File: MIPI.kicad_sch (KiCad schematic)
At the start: 14 parts, among them J14 AFC11-S30ICC-00, J15 AFC11-S30ICC-00

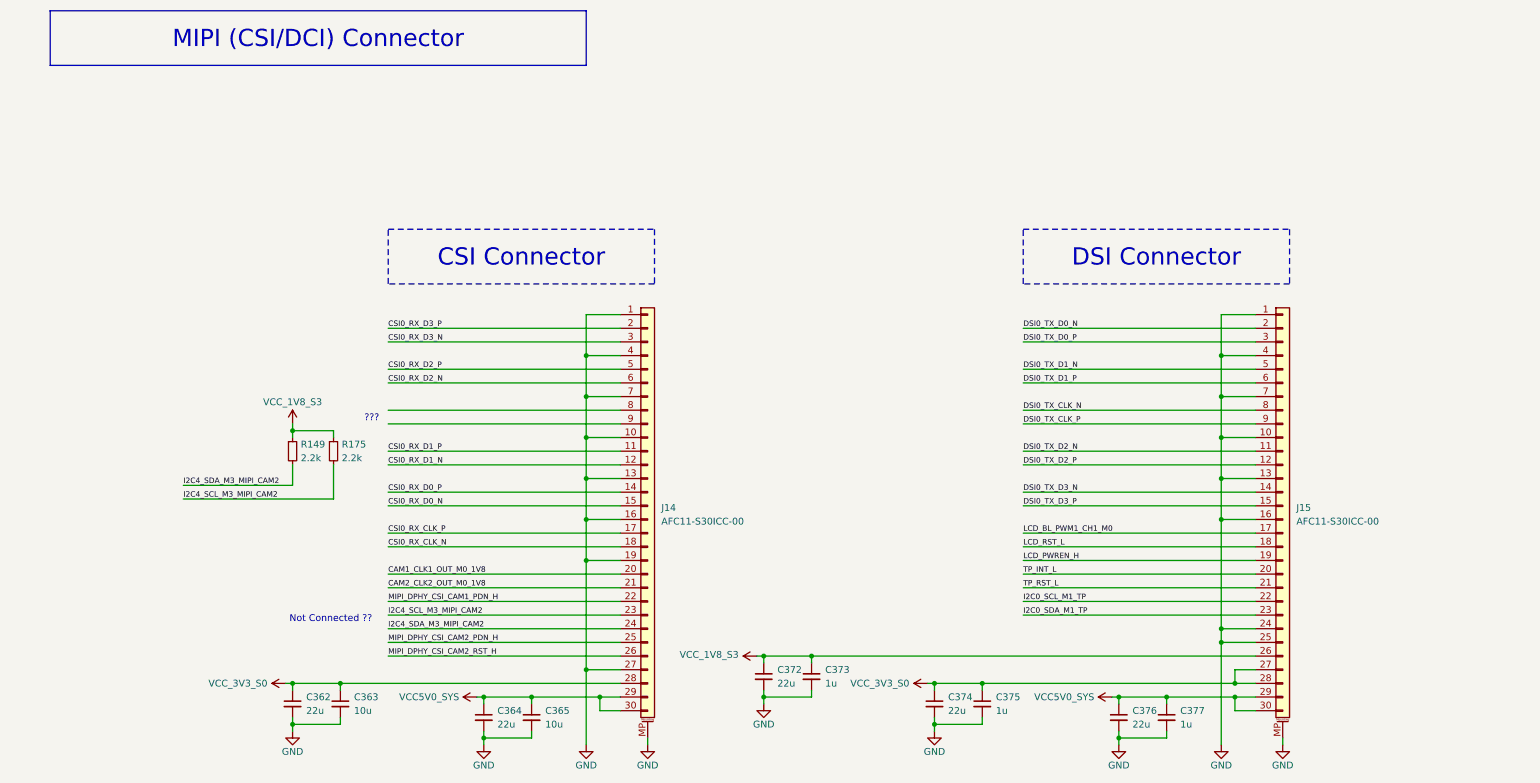
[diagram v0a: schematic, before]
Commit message: Replace v2 with updated RK3576_SBCv2 (Copy) Oct 2
- Update 18 sheets to Oct 2 15:37 local versions
- Keep cleaned layout: exclude .history/, Resources/, *.bak, *.lck,
  project.kicad_dru, .hs_rules.json, lowercase dup placeholders
  (fixtures/power), empty orphans (digital, mechanical, output,
  USBC_MCU, eMMC_UFS)
- Preserve LICENSE, README.md, .gitignore
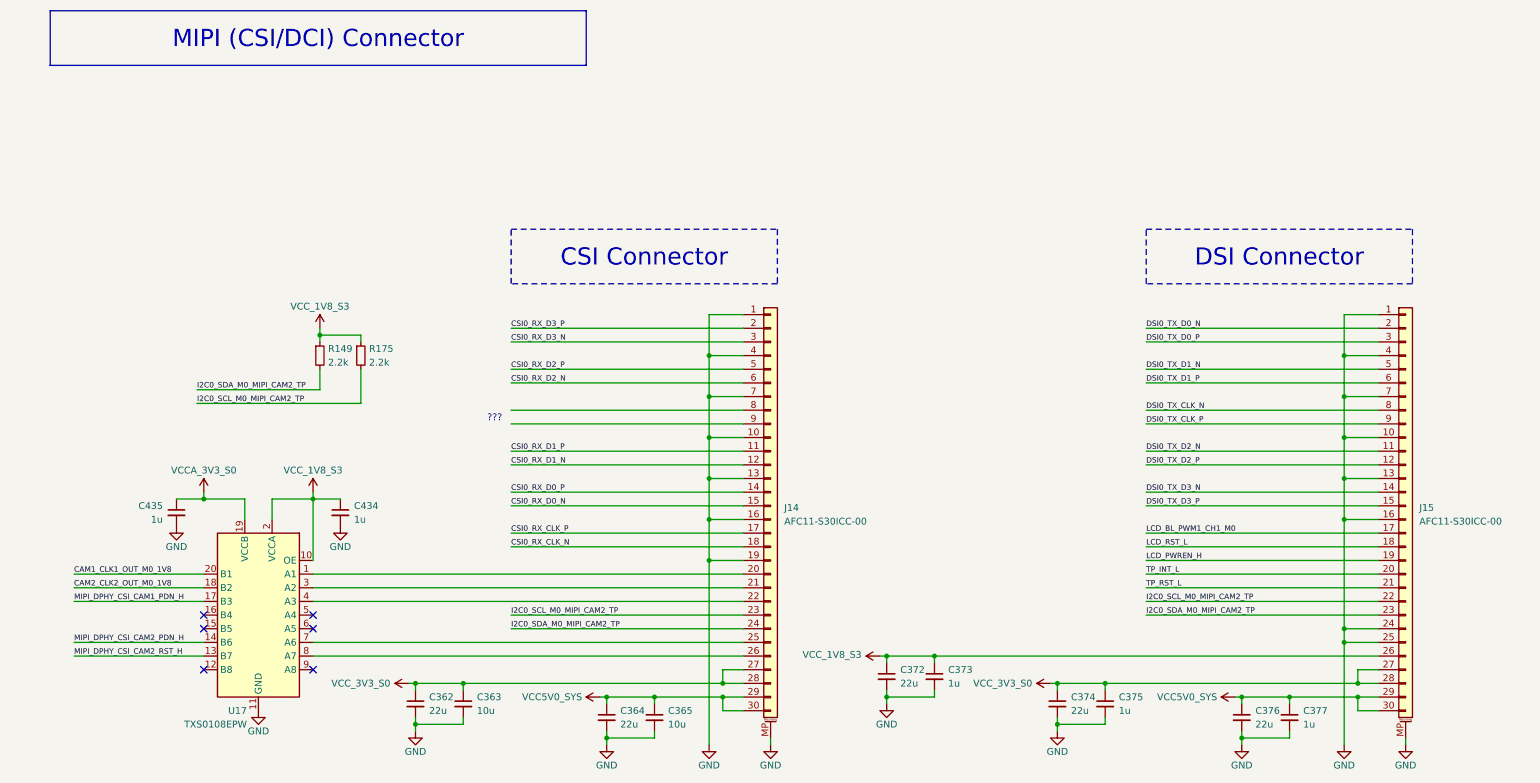
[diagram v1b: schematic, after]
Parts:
- added C434, C435: 1u, Capacitor_SMD:C_0201_0603Metric_Pad0.64x0.40mm_HandSolder, symbol New_Library_0:C_Small_edited
- added U17: TXS0108EPW, Datasheet_Footprints:TXS0108ERGYR_VQFN-20-EP_C90706, symbol Logic_LevelTranslator:TXS0108EPW
- C363, C365: footprint Capacitor_SMD:C_0201_0603Metric_Pad0.64x0.40mm_HandSolder -> Capacitor_SMD:C_0603_1608Metric; LCSC Part C5209398 -> C19702; Mouser Part CL03A105KP3NSNC -> 187-CL10A106KP8NNNC
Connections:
- net I2C4_SCL_M3_MIPI_CAM2 is gone; now on net I2C0_SCL_M0_MIPI_CAM2_TP: J14.23 (Pin_23), R175.2
- net I2C4_SDA_M3_MIPI_CAM2 is gone; now on net I2C0_SDA_M0_MIPI_CAM2_TP: J14.24 (Pin_24), R149.2
- net CAM1_CLK1_OUT_M0_1V8: now also U17.20 (B1); no longer J14.20 (Pin_20)
- net CAM2_CLK2_OUT_M0_1V8: now also U17.18 (B2); no longer J14.21 (Pin_21)
- net GND: now also C434.2, C435.2, U17.11 (GND); no longer J14.27 (Pin_27)
- net MIPI_DPHY_CSI_CAM1_PDN_H: now also U17.17 (B3); no longer J14.22 (Pin_22)
- net MIPI_DPHY_CSI_CAM2_PDN_H: now also U17.14 (B6); no longer J14.25 (Pin_25)
- net MIPI_DPHY_CSI_CAM2_RST_H: now also U17.13 (B7); no longer J14.26 (Pin_26)
- net VCC_1V8_S3: now also C434.1, U17.10 (OE), U17.2 (VCCA)
- net VCC_3V3_S0: now also J14.27 (Pin_27)
- net I2C0_SCL_M1_TP renamed I2C0_SCL_M0_MIPI_CAM2_TP
- net I2C0_SDA_M1_TP renamed I2C0_SDA_M0_MIPI_CAM2_TP
- new net: J14.20 (Pin_20), U17.1 (A1)
- new net: J14.21 (Pin_21), U17.3 (A2)
- new net: J14.22 (Pin_22), U17.4 (A3)
- new net: J14.25 (Pin_25), U17.7 (A6)
- new net: J14.26 (Pin_26), U17.8 (A7)
- new net VCCA_3V3_S0: C435.1, U17.19 (VCCB)
- no-connect marks 0 -> 6
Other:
- note removed: "Not Connected ??"
- moved on the sheet: C362, C363, C364, C365, C372, C373, C374, C375, C376, C377, J14, J15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

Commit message: Relink hierarchical root: 18 sheets into RK3576 SBCv2 top level
Root was empty (no sheet boxes); all subsheets orphaned.
Rebuilt A1 top level linking RK3576, LPDDR5, Power, Ethernet,
HDMI, MIPI, PCIe, USB-A/C, Wireless, RTC, uSD, GPIO, OLED,
RP2350A, Connectors, Fixtures, DC_Power. block_diagrame kept
docs-only (unlinked, avoids double-instantiation). Lowercase
stub duplicates excluded. ERC: 1388 -> 770 violations.
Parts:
- removed J14, J15: AFC11-S30ICC-00, easyeda2kicad:FPC-SMD_30P-L20.5-W2.0-P0.50, symbol Connector_Generic_MountingPin:Conn_01x30_MountingPin
- removed U17: TXS0108EPW, Datasheet_Footprints:TXS0108ERGYR_VQFN-20-EP_C90706, symbol Logic_LevelTranslator:TXS0108EPW
- added J16, J17: AFC11-S30ICC-00, easyeda2kicad:FPC-SMD_30P-L20.5-W2.0-P0.50, symbol Connector_Generic_MountingPin:Conn_01x30_MountingPin
- added U41: TXS0108EPW, Datasheet_Footprints:TXS0108ERGYR_VQFN-20-EP_C90706, symbol Logic_LevelTranslator:TXS0108EPW
- renumbered C435 to C252, C434 to C253, C362 to C254, C363 to C255, C364 to C256, C365 to C257, C372 to C258, C373 to C259, C374 to C260, C375 to C261, C376 to C262, C377 to C263, R149 to R185, R175 to R186
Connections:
- net CAM1_CLK1_OUT_M0_1V8: now also U41.20 (B1)
- net CAM2_CLK2_OUT_M0_1V8: now also U41.18 (B2)
- net CSI0_RX_CLK_N: now also J16.18 (Pin_18)
- net CSI0_RX_CLK_P: now also J16.17 (Pin_17)
- net CSI0_RX_D0_N: now also J16.15 (Pin_15)
- net CSI0_RX_D0_P: now also J16.14 (Pin_14)
- net CSI0_RX_D1_N: now also J16.12 (Pin_12)
- net CSI0_RX_D1_P: now also J16.11 (Pin_11)
- net CSI0_RX_D2_N: now also J16.6 (Pin_6)
- net CSI0_RX_D2_P: now also J16.5 (Pin_5)
- net CSI0_RX_D3_N: now also J16.3 (Pin_3)
- net CSI0_RX_D3_P: now also J16.2 (Pin_2)
- net DSI0_TX_CLK_N: now also J17.8 (Pin_8)
- net DSI0_TX_CLK_P: now also J17.9 (Pin_9)
- net DSI0_TX_D0_N: now also J17.2 (Pin_2)
- net DSI0_TX_D0_P: now also J17.3 (Pin_3)
- net DSI0_TX_D1_N: now also J17.5 (Pin_5)
- net DSI0_TX_D1_P: now also J17.6 (Pin_6)
- net DSI0_TX_D2_N: now also J17.11 (Pin_11)
- net DSI0_TX_D2_P: now also J17.12 (Pin_12)
- net DSI0_TX_D3_N: now also J17.14 (Pin_14)
- net DSI0_TX_D3_P: now also J17.15 (Pin_15)
- net GND: now also J16.1 (Pin_1), J16.10 (Pin_10), J16.13 (Pin_13), J16.16 (Pin_16), J16.19 (Pin_19), J16.4 (Pin_4), J16.7 (Pin_7), J16.MP (MountPin), J17.1 (Pin_1), J17.10 (Pin_10), J17.13 (Pin_13), J17.16 (Pin_16), J17.24 (Pin_24), J17.25 (Pin_25), J17.4 (Pin_4), J17.7 (Pin_7), J17.MP (MountPin), U41.11 (GND)
- net I2C0_SCL_M0_MIPI_CAM2_TP: now also J16.23 (Pin_23), J17.22 (Pin_22)
- net I2C0_SDA_M0_MIPI_CAM2_TP: now also J16.24 (Pin_24), J17.23 (Pin_23)
- net LCD_BL_PWM1_CH1_M0: now also J17.17 (Pin_17)
- net LCD_PWREN_H: now also J17.19 (Pin_19)
- net LCD_RST_L: now also J17.18 (Pin_18)
- net MIPI_DPHY_CSI_CAM1_PDN_H: now also U41.17 (B3)
- net MIPI_DPHY_CSI_CAM2_PDN_H: now also U41.14 (B6)
- net MIPI_DPHY_CSI_CAM2_RST_H: now also U41.13 (B7)
- net TP_INT_L: now also J17.20 (Pin_20)
- net TP_RST_L: now also J17.21 (Pin_21)
- net VCC5V0_SYS: now also J16.29 (Pin_29), J16.30 (Pin_30), J17.29 (Pin_29), J17.30 (Pin_30)
- net VCCA_3V3_S0: now also U41.19 (VCCB)
- net VCC_1V8_S3: now also J17.26 (Pin_26), U41.10 (OE), U41.2 (VCCA)
- net VCC_3V3_S0: now also J16.27 (Pin_27), J16.28 (Pin_28), J17.27 (Pin_27), J17.28 (Pin_28)
- new net: J16.20 (Pin_20), U41.1 (A1)
- new net: J16.21 (Pin_21), U41.3 (A2)
- new net: J16.22 (Pin_22), U41.4 (A3)
- new net: J16.25 (Pin_25), U41.7 (A6)
- new net: J16.26 (Pin_26), U41.8 (A7)

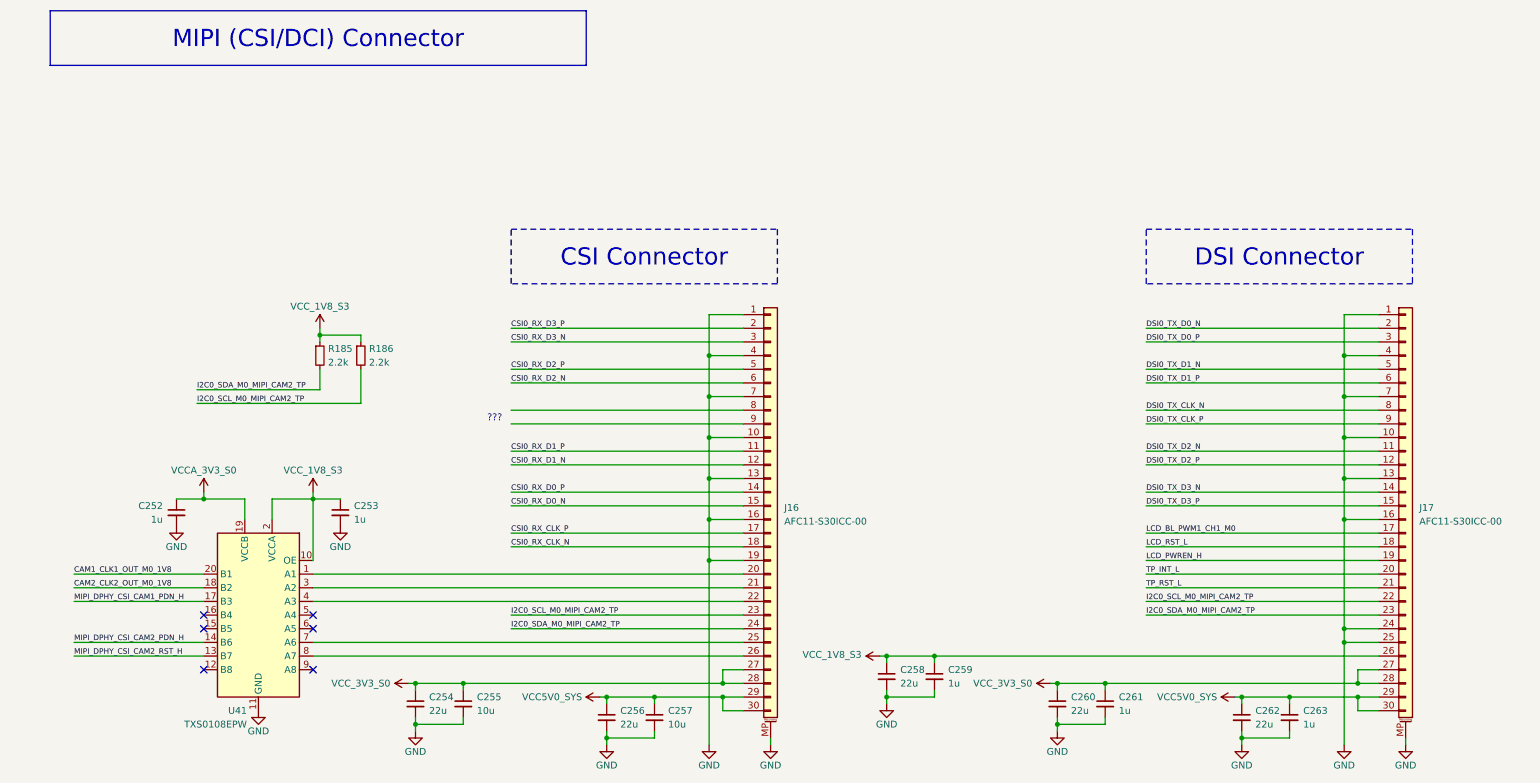
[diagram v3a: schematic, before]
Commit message: block diagrame with Hierarchical labels and NVMe SSD footprint
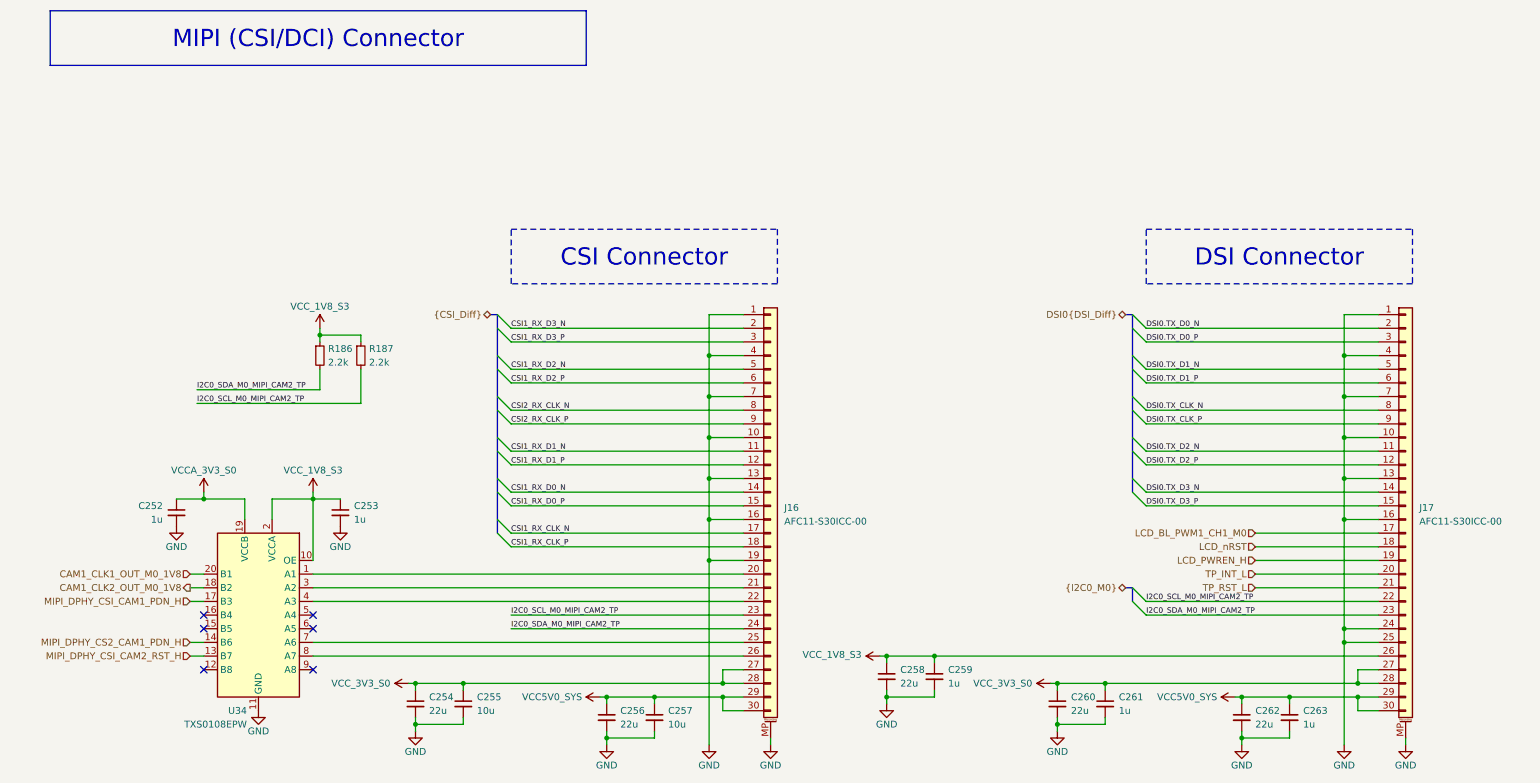
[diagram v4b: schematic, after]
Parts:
- renumbered R185 to R186, R186 to R187, U41 to U34
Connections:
- net CSI2_RX_CLK_N: now reaches J16.8 (Pin_8)
- net CSI2_RX_CLK_P: now reaches J16.9 (Pin_9)
- net CAM2_CLK2_OUT_M0_1V8 renamed CAM1_CLK2_OUT_M0_1V8
- net CSI0_RX_CLK_N renamed CSI1_RX_CLK_P
- net CSI0_RX_CLK_P renamed CSI1_RX_CLK_N
- net CSI0_RX_D0_N renamed CSI1_RX_D0_P
- net CSI0_RX_D0_P renamed CSI1_RX_D0_N
- net CSI0_RX_D1_N renamed CSI1_RX_D1_P
- net CSI0_RX_D1_P renamed CSI1_RX_D1_N
- net CSI0_RX_D2_N renamed CSI1_RX_D2_P
- net CSI0_RX_D2_P renamed CSI1_RX_D2_N
- net CSI0_RX_D3_N renamed CSI1_RX_D3_P
- net CSI0_RX_D3_P renamed CSI1_RX_D3_N
- net DSI0_TX_CLK_N renamed DSI0.TX_CLK_N
- net DSI0_TX_CLK_P renamed DSI0.TX_CLK_P
- net DSI0_TX_D0_N renamed DSI0.TX_D0_N
- net DSI0_TX_D0_P renamed DSI0.TX_D0_P
- net DSI0_TX_D1_N renamed DSI0.TX_D1_N
- net DSI0_TX_D1_P renamed DSI0.TX_D1_P
- net DSI0_TX_D2_N renamed DSI0.TX_D2_N
- net DSI0_TX_D2_P renamed DSI0.TX_D2_P
- net DSI0_TX_D3_N renamed DSI0.TX_D3_N
- net DSI0_TX_D3_P renamed DSI0.TX_D3_P
- net LCD_RST_L renamed LCD_nRST
- net MIPI_DPHY_CSI_CAM2_PDN_H renamed MIPI_DPHY_CS2_CAM1_PDN_H
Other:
- note removed: "???"
